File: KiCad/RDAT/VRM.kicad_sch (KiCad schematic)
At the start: 52 parts, among them M2 CSD17571Q2, M3 CSD17571Q2, Q3 PMOS, Q8 2N7002, SW1 SW_Push, SW2 SW_Push, U12 LTC4412xS6, U5 TPS54308, U7 TPS40345DRCR, U8 TPS54308

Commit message: Pre-Annotate FULL, add usb
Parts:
- Cvcc1: renamed from Cvcc; JLCPCB_LINK (none) -> https://jlcpcb.com/partdetail/MurataElectronics-GRM31CR71H4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

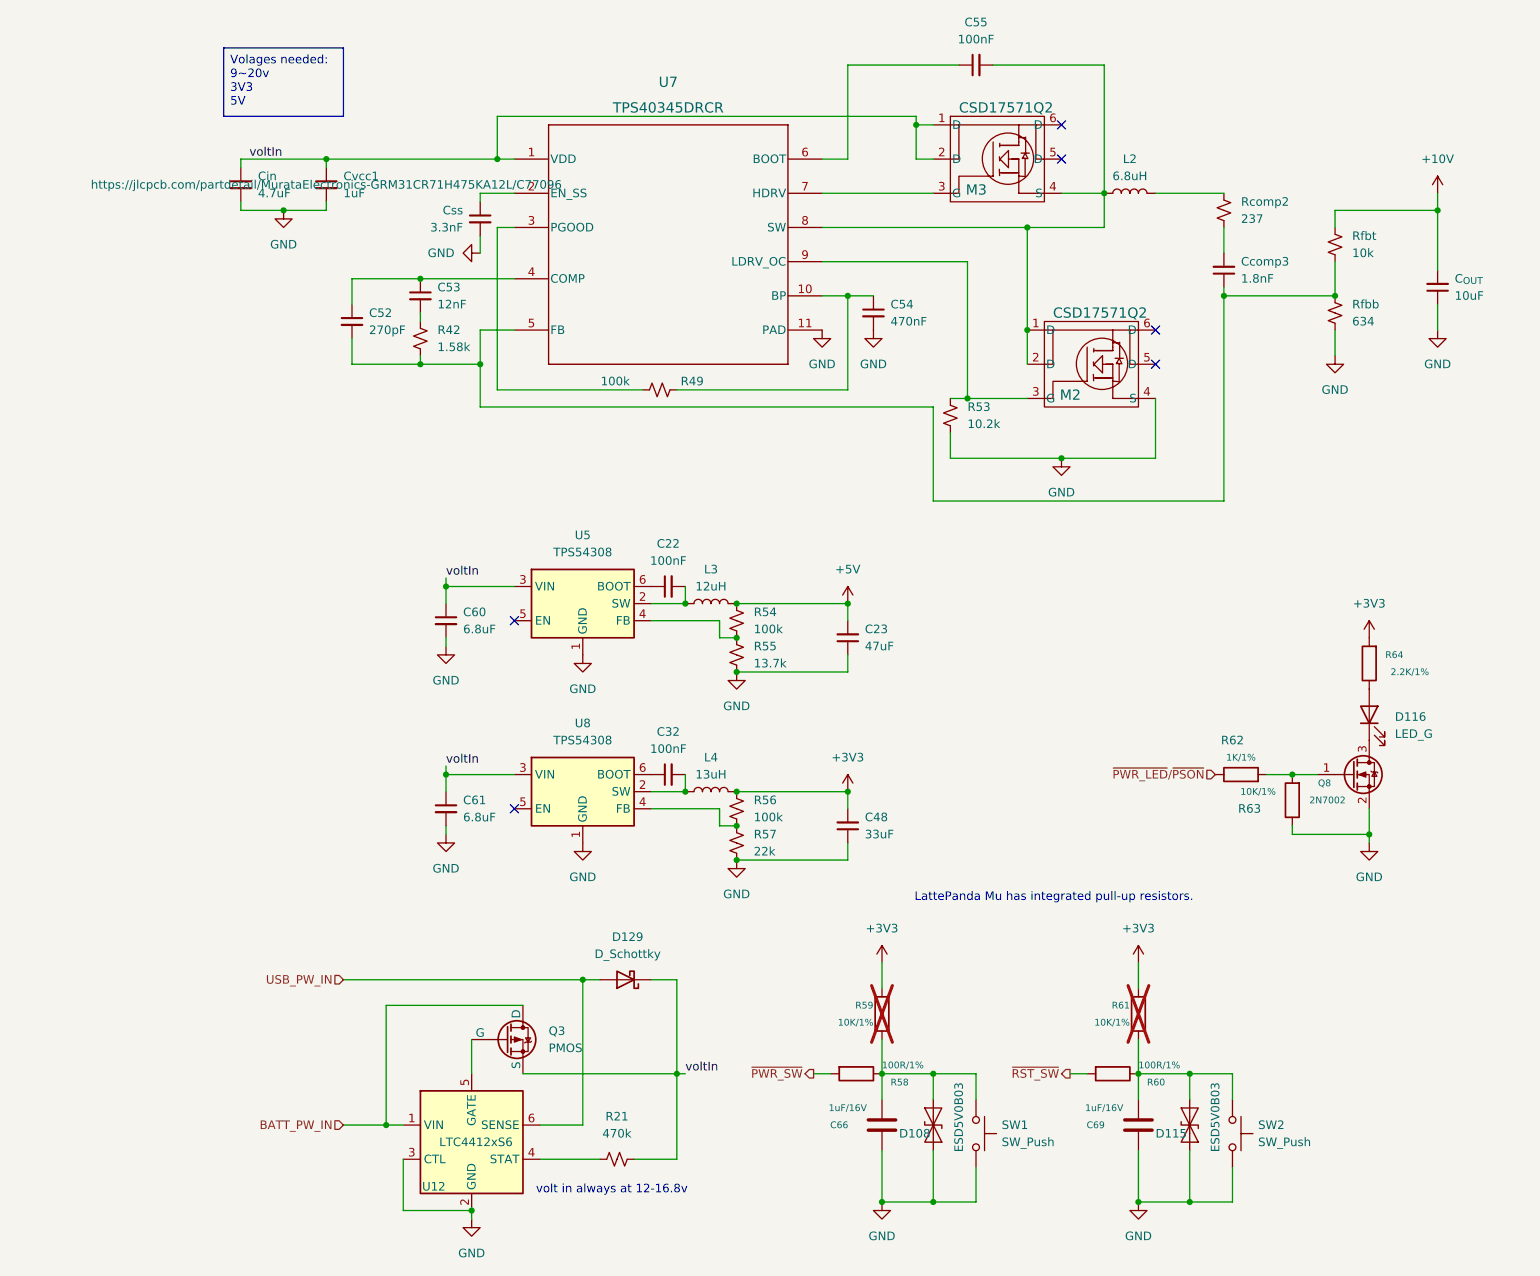
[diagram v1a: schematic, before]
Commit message: Added Libs and DOCS
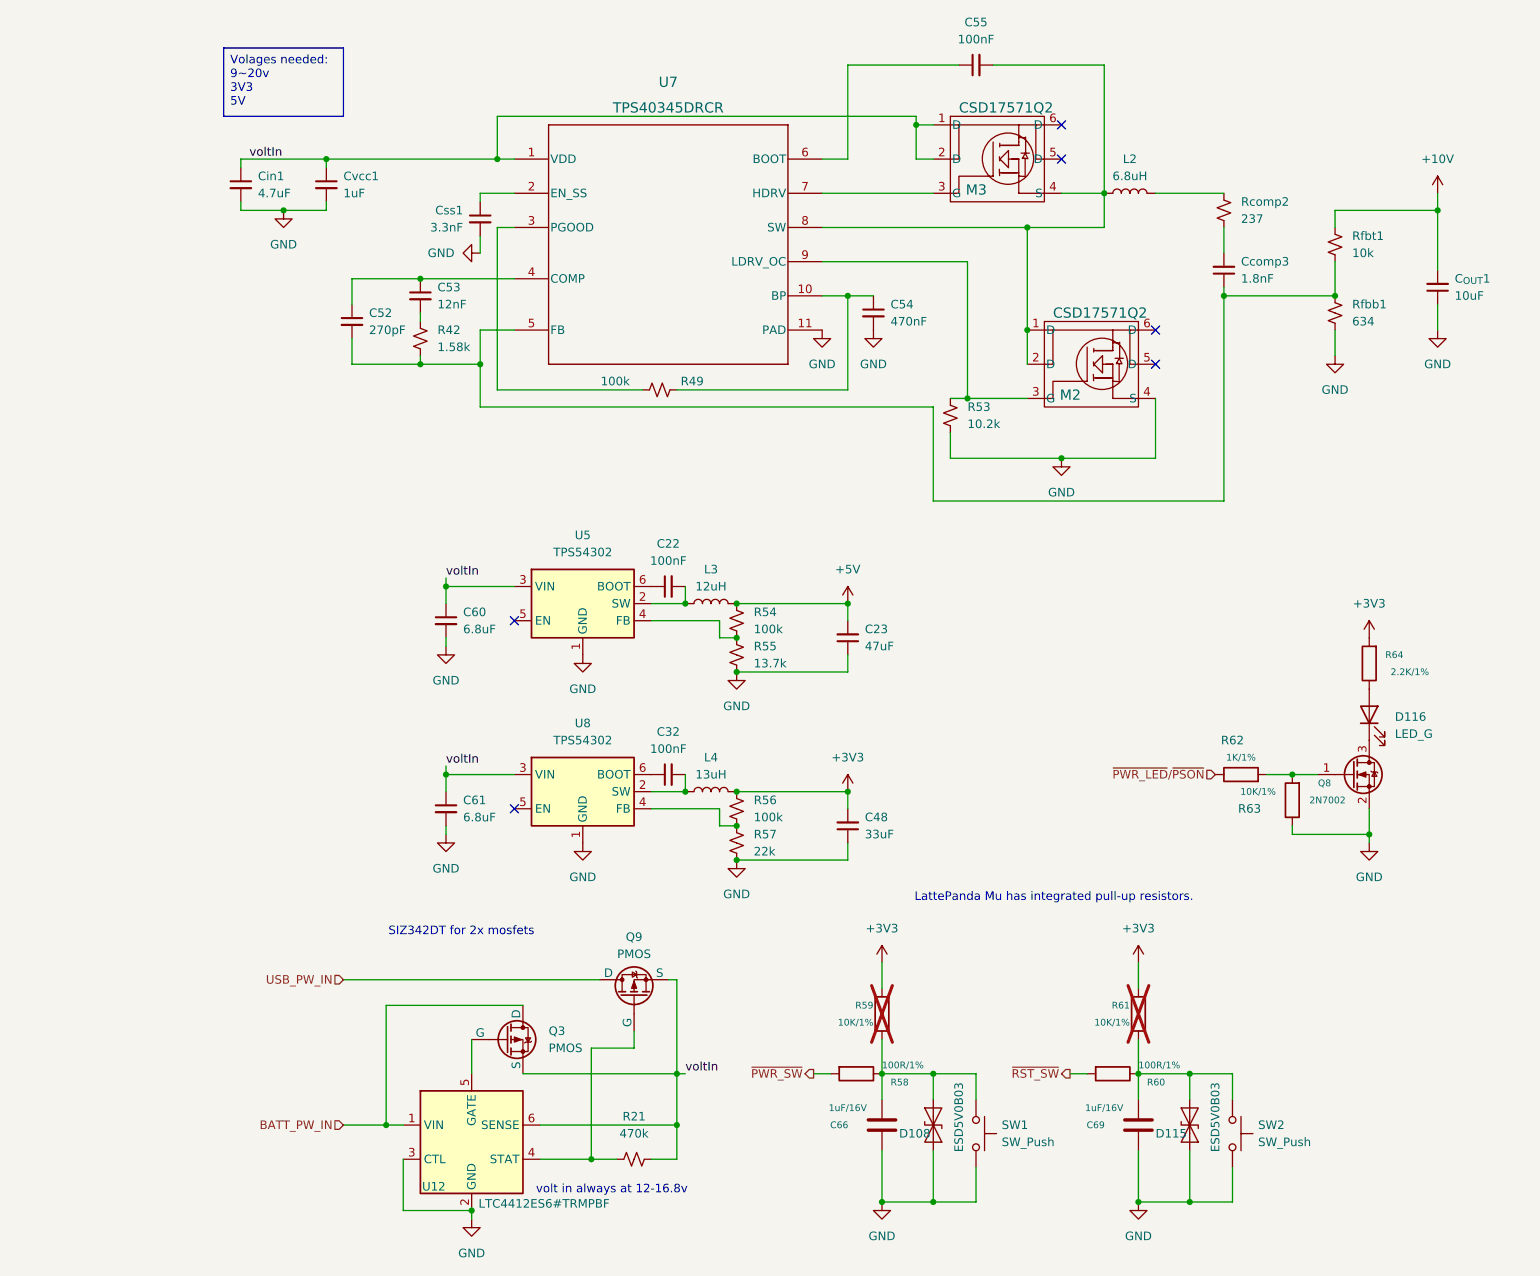
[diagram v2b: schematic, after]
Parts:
- removed D129: D_Schottky, symbol Device:D_Schottky
- added Q9: PMOS, symbol Simulation_SPICE:PMOS
- U12: value LTC4412xS6 -> LTC4412ES6#TRMPBF; JLCPCB_LINK (none) -> https://jlcpcb.com/partdetail/AnalogDevices-LTC4412ES6TRMPB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
- U5, U8: value TPS54308 -> TPS54302; JLCPCB_LINK (none) -> https://jlcpcb.com/partdetail/TexasInstruments-TPS54302DDCR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
- renumbered C_{OUT} to C_{OUT}1, Cin to Cin1, Css to Css1, Rfbb to Rfbb1, Rfbt to Rfbt1
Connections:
- net USB_PW_IN: now also Q9.1 (D); no longer U12.6 (SENSE)
- net voltIn: now also U12.6 (SENSE), Q9.3 (S)
- net at R21.1, U12.4 (STAT): now also Q9.2 (G)
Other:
- note added: "SIZ342DT for 2x mosfets"
- moved on the sheet: R21

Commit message: Sourced and documented all parts
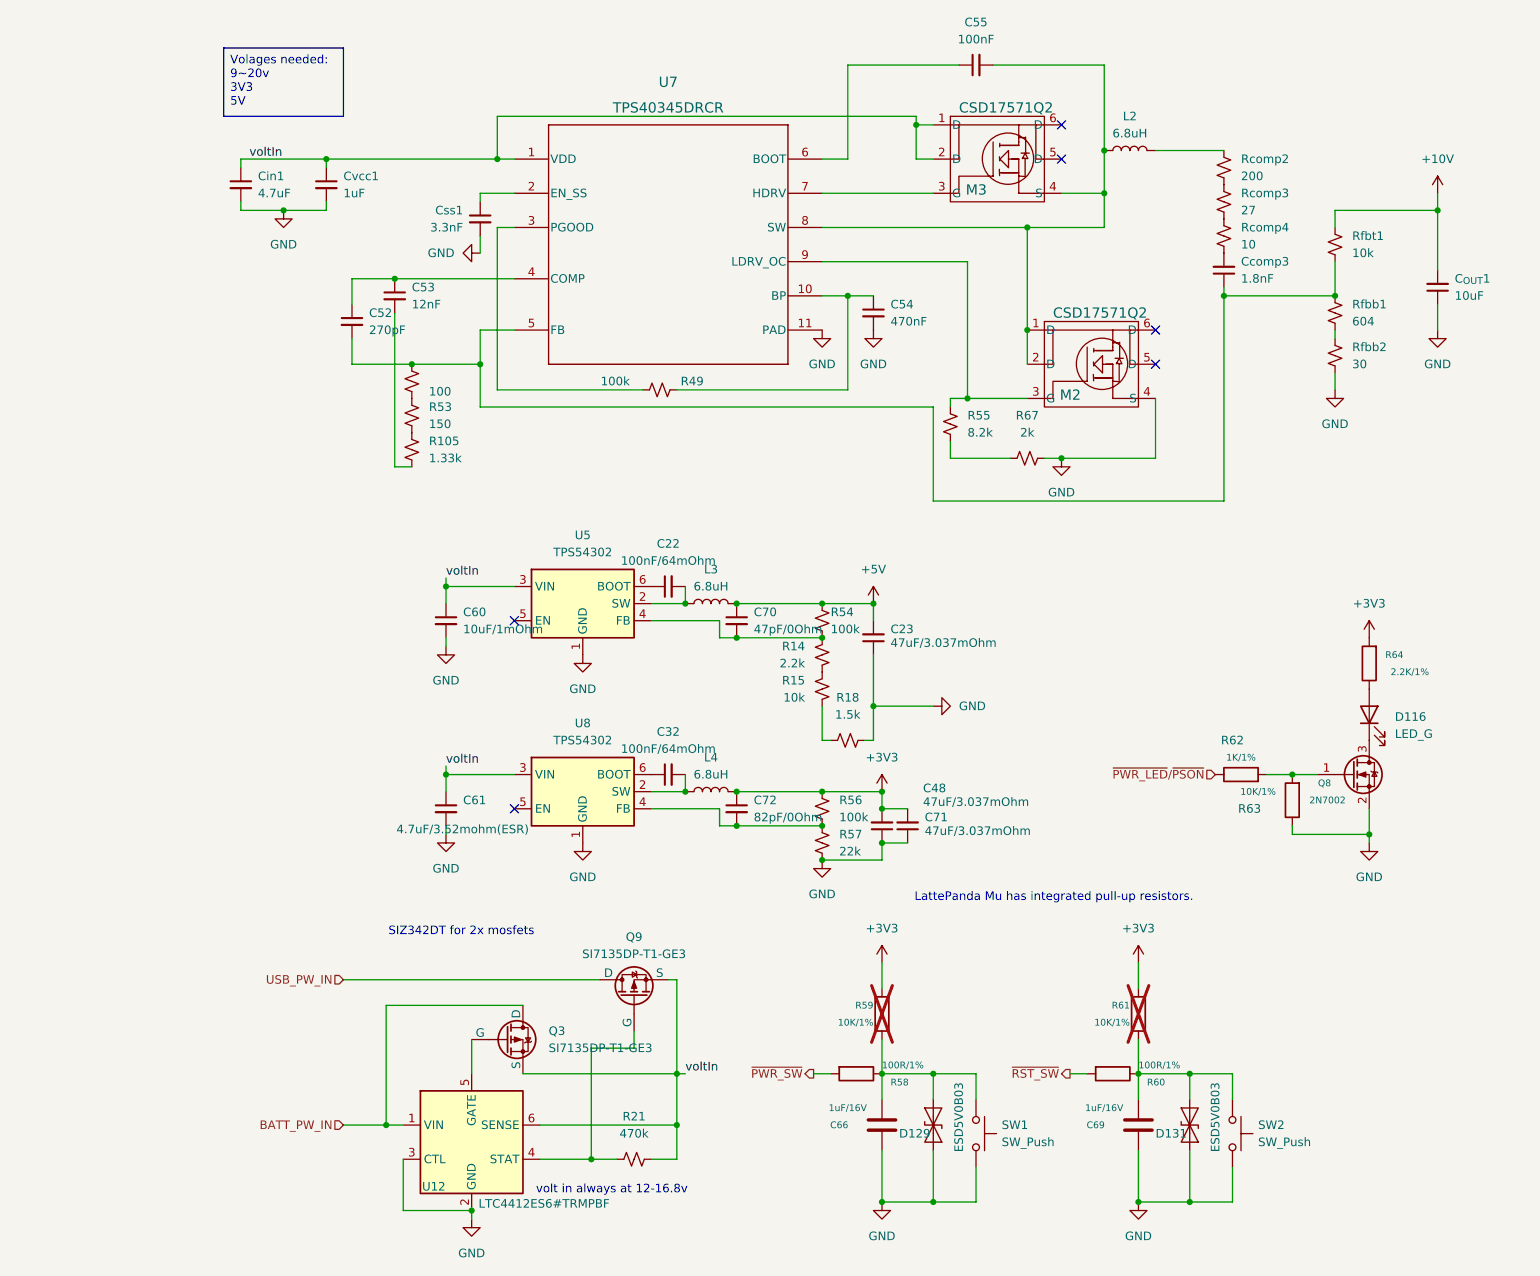
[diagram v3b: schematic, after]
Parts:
- removed D108, D115: ESD5V0B03, A_HDJ_Library:D_0402_1005Metric, symbol Diode:ESD9B5.0ST5G
- removed R42: 1.58k, symbol Device:R_Small_US
- added C70: 47pF/0Ohm, Capacitor_SMD:C_0402_1005Metric, symbol Device:C_Small
- added C71: 47uF/3.037mOhm, Capacitor_SMD:C_1210_3225Metric, symbol Device:C_Small
- added C72: 82pF/0Ohm, Capacitor_SMD:C_0201_0603Metric, symbol Device:C_Small
- added D129, D131: ESD5V0B03, Diode_SMD:D_SOD-882, symbol Diode:ESD9B5.0ST5G
- added R105: 1.33k, Resistor_SMD:R_0402_1005Metric, symbol Device:R_Small_US
- added R14: 2.2k, A_HDJ_Library:R_0402_1005Metric, symbol Device:R_Small_US
- added R15: 10k, Resistor_SMD:R_0402_1005Metric, symbol Device:R_Small_US
- added R18: 1.5k, A_HDJ_Library:R_0402_1005Metric, symbol Device:R_Small_US
- added R67: 2k, Resistor_SMD:R_0402_1005Metric, symbol Device:R_Small_US
- added R68: 100, Resistor_SMD:R_0402_1005Metric, symbol Device:R_Small_US
- added Rcomp3: 27, Resistor_SMD:R_0402_1005Metric, symbol Device:R_Small_US
- added Rcomp4: 10, Resistor_SMD:R_0402_1005Metric, symbol Device:R_Small_US
- added Rfbb2: 30, Resistor_SMD:R_0402_1005Metric, symbol Device:R_Small_US
- C22, C32: value 100nF -> 100nF/64mOhm; footprint (none) -> Capacitor_SMD:C_0402_1005Metric; JLCPCB_LINK (none) -> https://jlcpcb.com/partdetail/101286-CL05A104KA5NNNC/C100072
- C23: value 47uF -> 47uF/3.037mOhm; footprint (none) -> Capacitor_SMD:C_1210_3225Metric; JLCPCB_LINK (none) -> https://jlcpcb.com/partdetail/MurataElectronics-GRM32ER61C4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
- C48: value 33uF -> 47uF/3.037mOhm; footprint (none) -> Capacitor_SMD:C_1210_3225Metric; JLCPCB_LINK (none) -> https://jlcpcb.com/partdetail/MurataElectronics-GRM32ER61C4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
- C52: footprint (none) -> Capacitor_SMD:C_0201_0603Metric; JLCPCB_LINK (none) -> https://jlcpcb.com/partdetail/698284-GRM033R71E271KA01D/C66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
- C53: footprint (none) -> Capacitor_SMD:C_0402_1005Metric; JLCPCB_LINK (none) -> https://jlcpcb.com/partdetail/Yageo-CC0402KRX7R8BB123/C1137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
- C54: footprint (none) -> Capacitor_SMD:C_0402_1005Metric; JLCPCB_LINK (none) -> https://jlcpcb.com/partdetail/93554-CL05A474KA5NNNC/C92361
- C55: footprint (none) -> Capacitor_SMD:C_0402_1005Metric; JLCPCB_LINK (none) -> https://jlcpcb.com/partdetail/101286-CL05A104KA5NNNC/C100072
- C60: value 6.8uF -> 10uF/1mOhm; footprint (none) -> Capacitor_SMD:C_0402_1005Metric; JLCPCB_LINK (none) -> https://jlcpcb.com/partdetail/97651-CL10A106MA8NRNC/C96446
- C61: value 6.8uF -> 4.7uF/3.52mohm(ESR); footprint (none) -> Capacitor_SMD:C_0402_1005Metric; JLCPCB_LINK (none) -> https://jlcpcb.com/partdetail/Hre-CGA0402X5R475M250GT/C6119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
- C66, C69: JLCPCB_LINK (none) -> https://jlcpcb.com/partdetail/53938-CL05A105KA5NQNC/C52923
- C_{OUT}1: footprint (none) -> Capacitor_SMD:C_0402_1005Metric; JLCPCB_LINK (none) -> https://jlcpcb.com/partdetail/97651-CL10A106MA8NRNC/C96446
- Ccomp3: footprint (none) -> Capacitor_SMD:C_0402_1005Metric; JLCPCB_LINK (none) -> https://jlcpcb.com/partdetail/5718-CL05B182KB5NNNC/C5296
- Cin1: footprint (none) -> Capacitor_SMD:C_0402_1005Metric; JLCPCB_LINK (none) -> https://jlcpcb.com/partdetail/Hre-CGA0402X5R475M250GT/C6119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
- Css1: footprint (none) -> Capacitor_SMD:C_0402_1005Metric; JLCPCB_LINK (none) -> https://jlcpcb.com/partdetail/53938-CL05A105KA5NQNC/C52923
- Cvcc1: footprint (none) -> Capacitor_SMD:C_1206_3216Metric
- D116: JLCPCB_LINK (none) -> https://jlcpcb.com/partdetail/Silverlight-P0603P1N46G12/C51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
- L2: footprint (none) -> Inductor_SMD:L_Vishay_IHLP-2525; JLCPCB_LINK (none) -> https://jlcpcb.com/partdetail/VishayIntertech-IHLP2525CZER6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
- L3: value 12uH -> 6.8uH; footprint (none) -> Inductor_SMD:L_Vishay_IHLP-2525; JLCPCB_LINK (none) -> https://jlcpcb.com/partdetail/VishayIntertech-IHLP2525CZER6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
- L4: value 13uH -> 6.8uH; footprint (none) -> Inductor_SMD:L_Vishay_IHLP-2525; JLCPCB_LINK (none) -> https://jlcpcb.com/partdetail/VishayIntertech-IHLP2525CZER6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
- M2, M3: footprint DQK0006C -> Package_SON:WSON-6-1EP_2x2mm_P0.65mm_EP1x1.6mm_ThermalVias; JLCPCB_LINK (none) -> https://jlcpcb.com/partdetail/TexasInstruments-CSD17571Q2/C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
- Q3, Q9: value PMOS -> SI7135DP-T1-GE3; footprint (none) -> Package_SO:PowerPAK_SO-8_Single; JLCPCB_LINK (none) -> https://jlcpcb.com/partdetail/VishayIntertech-SI7135DP_T1GE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
- Q8: JLCPCB_LINK (none) -> https://jlcpcb.com/partdetail/9040-2N7002/C8545
- R21: footprint (none) -> A_HDJ_Library:R_0402_1005Metric; JLCPCB_LINK (none) -> https://jlcpcb.com/partdetail/26533-0402WGF4703TCE/C25790
- R49, R54, R56: footprint (none) -> A_HDJ_Library:R_0402_1005Metric; JLCPCB_LINK (none) -> https://jlcpcb.com/partdetail/26484-0402WGF1003TCE/C25741
- R53: value 10.2k -> 150; footprint (none) -> Resistor_SMD:R_0402_1005Metric; JLCPCB_LINK (none) -> https://jlcpcb.com/partdetail/25825-0402WGF1500TCE/C25082
- R55: value 13.7k -> 8.2k; footprint (none) -> Capacitor_SMD:C_0402_1005Metric; JLCPCB_LINK (none) -> https://jlcpcb.com/partdetail/26667-0402WGF8201TCE/C25924
- R57: footprint (none) -> Resistor_SMD:R_0402_1005Metric; JLCPCB_LINK (none) -> https://jlcpcb.com/partdetail/26511-0402WGF2202TCE/C25768
- R58, R60: JLCPCB_LINK (none) -> https://jlcpcb.com/partdetail/25819-0402WGF1000TCE/C25076
- R62: JLCPCB_LINK (none) -> https://jlcpcb.com/partdetail/12256-0402WGF1001TCE/C11702
- R63: JLCPCB_LINK (none) -> https://jlcpcb.com/partdetail/26487-0402WGF1002TCE/C25744
- R64: JLCPCB_LINK (none) -> https://jlcpcb.com/partdetail/26622-0402WGF2201TCE/C25879
- Rcomp2: value 237 -> 200; footprint (none) -> Resistor_SMD:R_0402_1005Metric; JLCPCB_LINK (none) -> https://jlcpcb.com/partdetail/25830-0402WGF2000TCE/C25087
- Rfbb1: value 634 -> 604; footprint (none) -> Resistor_SMD:R_0402_1005Metric; JLCPCB_LINK (none) -> https://jlcpcb.com/partdetail/8863-0402WGF6040TCE/C8369
- Rfbt1: footprint (none) -> Resistor_SMD:R_0402_1005Metric; JLCPCB_LINK (none) -> https://jlcpcb.com/partdetail/26487-0402WGF1002TCE/C25744
- SW1, SW2: footprint A_HDJ_Library:SW_Push_6x6x6 -> footprints:SW_TS-1187A-B-A-B; JLCPCB_LINK (none) -> https://jlcpcb.com/partdetail/XkbConnection-TS_1187A_B_AB/C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
- U7: JLCPCB_LINK (none) -> https://jlcpcb.com/partdetail/TexasInstruments-TPS40345DRCR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
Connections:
- net +3V3: now also C71.2, C72.1
- net +5V: now also C70.1
- net GND: now also C71.1, D129.1 (A1), D131.1 (A1), R18.2, R67.1, Rfbb2.1; no longer R53.1, R55.2, Rfbb1.1
- net at C66.1, R58.1, R59.1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: now also D129.2 (A2)
- net at C69.1, R60.1, R61.1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: now also D131.2 (A2)
- net at R56.2, R57.1, U8.4 (FB): now also C72.2
- net at C52.2, Ccomp3.1, Rfbb1.2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: now also R68.1
- net at M2.3 (G), U7.9 (LDRV_OC): now also R55.2; no longer R53.2
- net at C53.2: now also R105.2
- net at R54.2, U5.4 (FB): now also C70.2, R14.1; no longer R55.1
- net at Ccomp3.2: now also Rcomp4.1; no longer Rcomp2.1
- new net: R53.1, R68.2
- new net: Rfbb1.1, Rfbb2.2
- new net: Rcomp3.1, Rcomp4.2
- new net: R14.2, R15.1
- new net: R15.2, R18.1
- new net: Rcomp2.1, Rcomp3.2
- new net: R55.1, R67.2
- new net: R105.1, R53.2
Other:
- moved on the sheet: C23, C53, L2, R54, R56, R57, Rcomp2

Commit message: Push before Board Layout
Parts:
- C66, C69: footprint A_HDJ_Library:C_0402_1005Metric -> Capacitor_SMD:C_0402_1005Metric
- D116: footprint A_HDJ_Library:LED_0603_1608Metric -> LED_SMD:LED_0603_1608Metric
- Q8: footprint A_HDJ_Library:SOT-23 -> Package_TO_SOT_SMD:SOT-23
- R14, R18, R21, R49, R54, R56, R58, R60, R62, R63, R64: footprint A_HDJ_Library:R_0402_1005Metric -> Resistor_SMD:R_0402_1005Metric
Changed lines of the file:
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@@
 			)
 		)
-		(property "Footprint" "A_HDJ_Library:C_0402_1005Metric"
+		(property "Footprint" "Capacitor_SMD:C_0402_1005Metric"
 			(at 113.9952 179.07 0)
 			(effects
@@
 			)
 		)
-		(property "Footprint" "A_HDJ_Library:R_0402_1005Metric"
+		(property "Footprint" "Resistor_SMD:R_0402_1005Metric"
 			(at 175.768 127 90)
 			(effects
@@
 			)
 		)
-		(property "Footprint" "A_HDJ_Library:R_0402_1005Metric"
+		(property "Footprint" "Resistor_SMD:R_0402_1005Metric"
 			(at 187.198 106.68 90)
 			(effects
@@
 			)
 		)
-		(property "Footprint" "A_HDJ_Library:R_0402_1005Metric"
+		(property "Footprint" "Resistor_SMD:R_0402_1005Metric"
 			(at 147.32 165.862 90)
 			(effects
@@
 			)
 		)
-		(property "Footprint" "A_HDJ_Library:R_0402_1005Metric"
+		(property "Footprint" "Resistor_SMD:R_0402_1005Metric"
 			(at 80.01 66.04 0)
 			(effects
@@
 			)
 		)
-		(property "Footprint" "A_HDJ_Library:R_0402_1005Metric"
+		(property "Footprint" "Resistor_SMD:R_0402_1005Metric"
 			(at 109.22 165.862 90)
 			(effects
@@
 			)
 		)
-		(property "Footprint" "A_HDJ_Library:R_0402_1005Metric"
+		(property "Footprint" "Resistor_SMD:R_0402_1005Metric"
 			(at 104.14 128.27 0)
 			(effects
@@
 			)
 		)
-		(property "Footprint" "A_HDJ_Library:R_0402_1005Metric"
+		(property "Footprint" "Resistor_SMD:R_0402_1005Metric"
 			(at 104.14 100.33 0)
 			(effects
@@
 			)
 		)
-		(property "Footprint" "A_HDJ_Library:LED_0603_1608Metric"
+		(property "Footprint" "LED_SMD:LED_0603_1608Metric"
 			(at 185.42 114.3 0)
 			(effects
@@
 			)
 		)
-		(property "Footprint" "A_HDJ_Library:SOT-23"
+		(property "Footprint" "Package_TO_SOT_SMD:SOT-23"
 			(at 187.96 125.095 0)
 			(effects
@@
 			)
 		)
-		(property "Footprint" "A_HDJ_Library:R_0402_1005Metric"
+		(property "Footprint" "Resistor_SMD:R_0402_1005Metric"
 			(at 107.95 118.11 0)
 			(effects
@@
 			)
 		)
-		(property "Footprint" "A_HDJ_Library:R_0402_1005Metric"
+		(property "Footprint" "Resistor_SMD:R_0402_1005Metric"
 			(at 166.37 124.968 90)
 			(effects
@@
 			)
 		)
-		(property "Footprint" "A_HDJ_Library:R_0402_1005Metric"
+		(property "Footprint" "Resistor_SMD:R_0402_1005Metric"
 			(at 104.14 105.41 0)
 			(effects
@@
 			)
 		)
-		(property "Footprint" "A_HDJ_Library:C_0402_1005Metric"
+		(property "Footprint" "Capacitor_SMD:C_0402_1005Metric"
 			(at 152.0952 179.07 0)
 			(effects
@@
 			)
 		)
-		(property "Footprint" "A_HDJ_Library:R_0402_1005Metric"
+		(property "Footprint" "Resistor_SMD:R_0402_1005Metric"
 			(at 76.2 180.34 0)
 			(effects

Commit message: Placed a lot of components
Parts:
- removed SW1, SW2: SW_Push, footprints:SW_TS-1187A-B-A-B, symbol Switch:SW_Push
- added S104, S105: TS-1187A-B-A-B, footprints:SW_TS-1187A-B-A-B, symbol TS-1187A-B-A-B:TS-1187A-B-A-B
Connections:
- net GND: now also S104.C, S104.D, S105.C, S105.D
- net at C66.1, D129.2 (A2), R58.1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: now also S104.A, S104.B
- net at C69.1, D131.2 (A2), R60.1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: now also S105.A, S105.B
- net at C55.2, L2.1, M3.4 (S)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: now also M2.5 (D), M2.6 (D); no longer M2.1 (D), M2.2 (D)
- no-connect marks 6 -> 7
